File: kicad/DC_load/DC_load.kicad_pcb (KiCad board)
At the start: 2 copper layers, 110 x 145 mm, 217 parts, among them J1 BNC, J10 DC fan connector, J2 red_terminal, J3 red terminal, J4 black terminal, J5 black terminal, J6 USB_B, J8 FT232 programming port, J9 Conn_01x04_Socket, Q1 MMBT5401, Q10 MMBT5401, Q11 MMBT5551L, Q12 MMBT5401, Q13 AO3400A, Q14 MMBT5551L, Q2 MMBT5401, Q3 FQP19N20C, Q4 FQP19N20C, Q5 FQP19N20C, Q6 FQP19N20C, Q7 MMBT5551L, Q8 MMBT5401, Q9 MMBT5551L, SW1 RotaryEncoder_Switch, SW2 RotaryEncoder_Switch, SW3 SW_Push, SW8 SW_Push, U1 FSA3157P6X, U10 FSA3157P6X, U11 FSA3157P6X, U12 FSA3157P6X, U13 TLV9062, U14 AMS1117-3.3, U15 74HC14D653, U16 93LCxxB, U17 CH340C, U18 TL431DBZ, U19 INA181, U2 Screen, U20 INA181, U21 INA181, U22 INA181, U5 TLV9062, U6 TLV9062, U7 LMT84LPM, U8 STM32F103C8Tx, U9 Front plate

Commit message: Još gate driver layout.
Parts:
- removed TP10: TestPoint, TestPoint:TestPoint_Pad_D2.0mm
- moved JP3 6.55 mm to (95.1, 117.4), turned to 180 degrees
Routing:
- net /Microcontroller/BNC_CONTROL: track 120.8 -> 45.8 mm
- net CTRL_SEL: track 186.1 -> 117.3 mm
- net FAN_PWM: track 0.00 -> 61.4 mm, vias 0 -> 3
- net 3V3: track 113.0 -> 104.5 mm
- net /Microcontroller/CH3_MEAS: track 138.2 -> 130.0 mm
- net CH1_CONTROL: track 6.50 -> 0.00 mm
- net Net-(C26-Pad2): track 103.6 -> 97.4 mm
- net 5V: track 102.7 -> 96.6 mm
- net CH2_CONTROL: track 4.52 -> 0.00 mm
- net Net-(Q3-S): track 6.17 -> 3.48 mm
- net Net-(Q6-S): track 6.24 -> 4.31 mm
- net GND: track 120.3 -> 119.2 mm
- net Net-(R22-Pad2): track 29.8 -> 28.8 mm
- net Net-(R23-Pad2): track 30.6 -> 29.7 mm
- net Net-(Q5-S): track 3.65 -> 2.93 mm
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
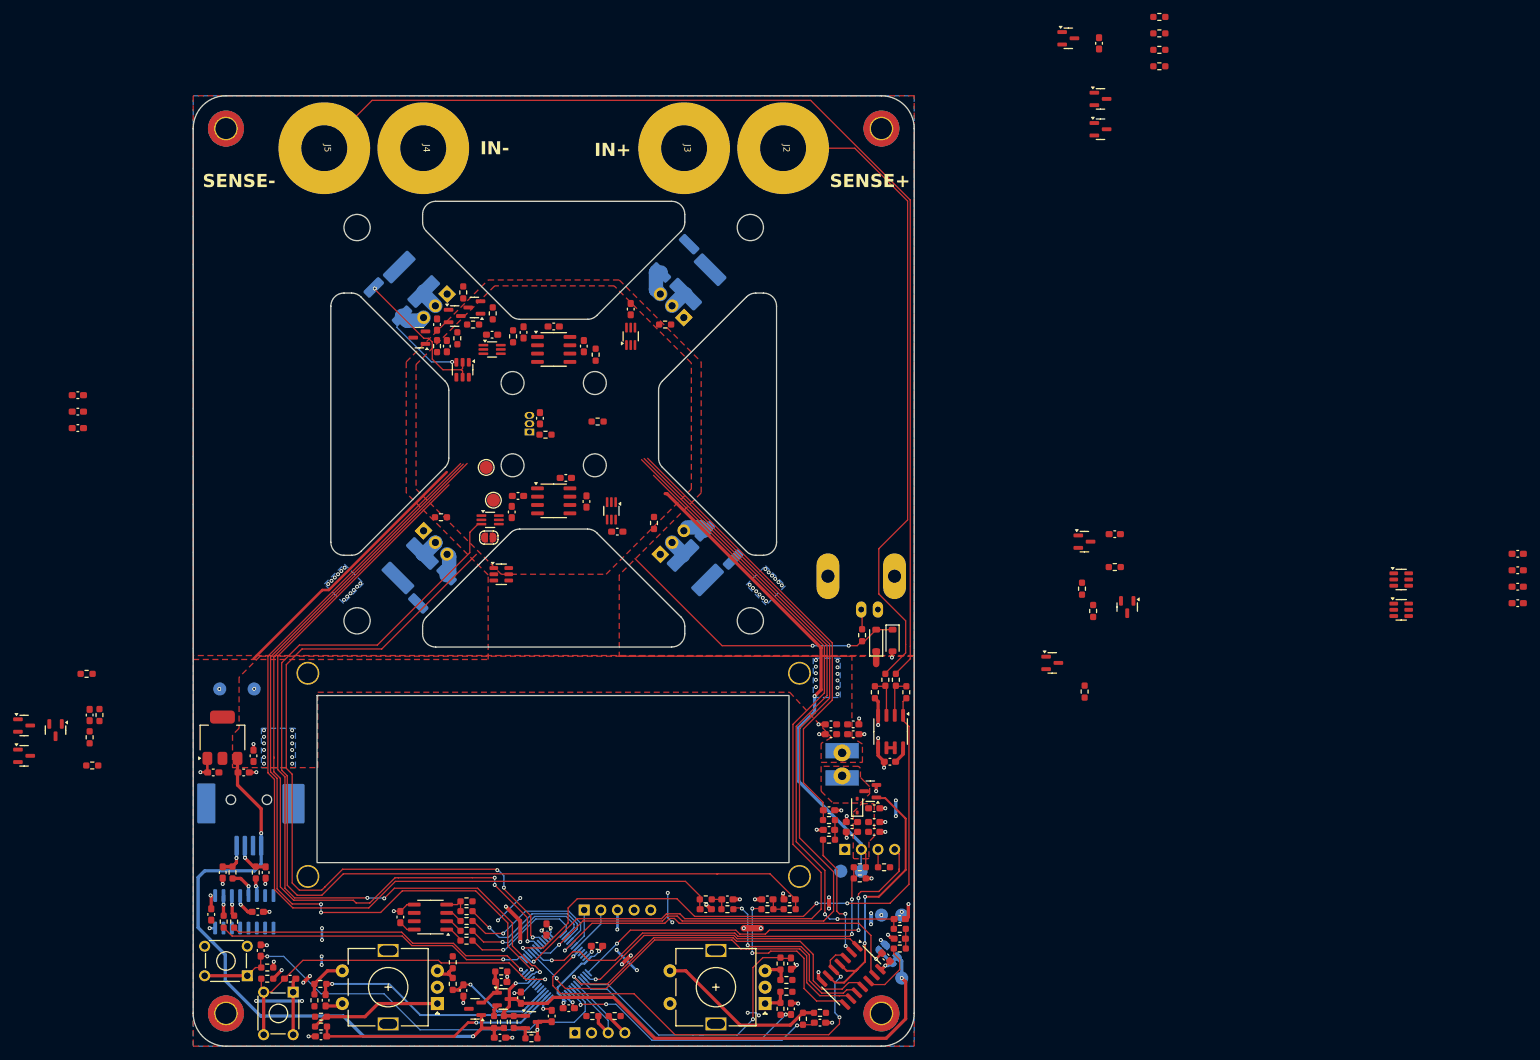
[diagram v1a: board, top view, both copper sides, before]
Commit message: RC filter na ADC linijama Placement update.
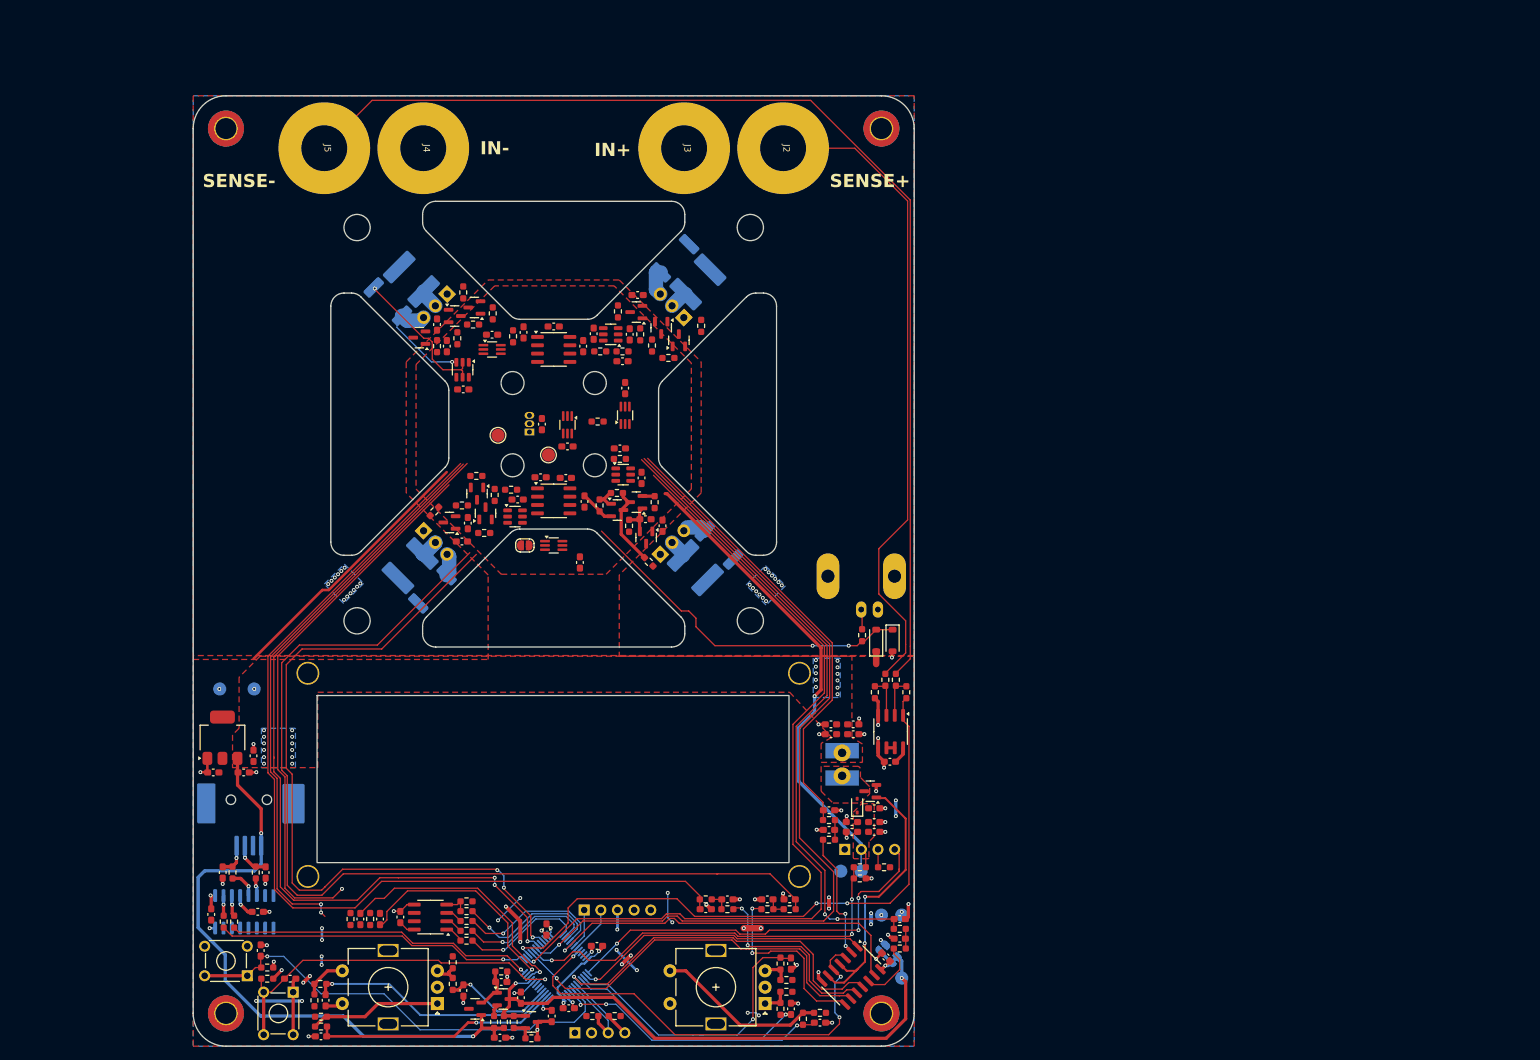
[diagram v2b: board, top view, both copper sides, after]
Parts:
- added C70: 1n, Capacitor_SMD:C_0603_1608Metric_Pad1.08x0.95mm_HandSolder, F.Cu at (115.5, 90.5)
- added C71: 1n, Capacitor_SMD:C_0603_1608Metric_Pad1.08x0.95mm_HandSolder, F.Cu at (115.1, 103.8)
- added C72: 1n, Capacitor_SMD:C_0603_1608Metric_Pad1.08x0.95mm_HandSolder, F.Cu at (78.5, 175.6)
- added C73: 1n, Capacitor_SMD:C_0603_1608Metric_Pad1.08x0.95mm_HandSolder, F.Cu at (75.5, 175.6)
- added R75: 10k, Resistor_SMD:R_0603_1608Metric_Pad0.98x0.95mm_HandSolder, F.Cu at (74.0, 175.6)
- added R76: 10k, Resistor_SMD:R_0603_1608Metric_Pad0.98x0.95mm_HandSolder, F.Cu at (77.0, 175.6)
- added R77: 10k, Resistor_SMD:R_0603_1608Metric_Pad0.98x0.95mm_HandSolder, F.Cu at (115.1, 105.4)
- added R78: 10k, Resistor_SMD:R_0603_1608Metric_Pad0.98x0.95mm_HandSolder, F.Cu at (115.5, 89.0)
- moved C9 162.8 mm to (91.2, 94.8)
- moved C65 153.4 mm to (99.5, 111.6)
- moved C46 145.5 mm to (111.1, 86.3), turned to -90 degrees
- moved C64 134.7 mm to (118.4, 108.3), turned to 90 degrees
- moved U22 127.7 mm to (113.7, 86.4), turned to 180 degrees
- moved U21 119.8 mm to (115.6, 107.8)
- moved R71 92.8 mm to (118.2, 86.4), turned to -90 degrees
- moved C68 90.9 mm to (121.6, 115.6), turned to -90 degrees
- moved R72 90.9 mm to (120.0, 88.1), turned to -90 degrees
- moved R74 90.7 mm to (114.8, 82.9), turned to -90 degrees
- moved R73 88.4 mm to (122.5, 90.0)
- moved C67 84.7 mm to (116.6, 86.4), turned to -90 degrees
- moved C7 80.2 mm to (117.8, 80.4), turned to 0 degrees
- moved Q7 79.8 mm to (93.3, 110.7), turned to -90 degrees
- moved D8 78.0 mm to (117.6, 83.0), turned to 180 degrees
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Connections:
- net /Microcontroller/PROG_RX renamed PROG_RX
- net /Microcontroller/PROG_TX renamed PROG_TX
- C16 pad 2: 5V -> 3V3
- C17 pad 2: 5V -> 3V3
- C18 pad 2: 5V -> 3V3
- C19 pad 2: 5V -> 3V3
- U1 pad 5: 5V -> 3V3
- U10 pad 5: 5V -> 3V3
- U11 pad 5: 5V -> 3V3
- U12 pad 5: 5V -> 3V3
- U8 pad 10: /Microcontroller/CH1_MEAS -> Net-(U8-PA0)
- U8 pad 11: /Microcontroller/CH2_MEAS -> Net-(U8-PA1)
- U8 pad 14: /Microcontroller/CH3_MEAS -> Net-(U8-PA4)
- U8 pad 18: /Microcontroller/CH4_MEAS -> Net-(U8-PB0)
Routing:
- net Net-(U8-PB0): track 0.00 -> 133.8 mm
- net /Microcontroller/CH4_MEAS: track 133.8 -> 0.00 mm
- net Net-(U8-PA4): track 0.00 -> 130.0 mm
- net /Microcontroller/CH3_MEAS: track 130.0 -> 0.00 mm
- net /Microcontroller/CH2_MEAS: track 128.1 -> 0.00 mm, vias 3 -> 1
- net Net-(U8-PA1): track 0.00 -> 121.2 mm, vias 0 -> 2
- net /Microcontroller/CH1_MEAS: track 122.5 -> 82.7 mm, vias 3 -> 2
- net Net-(U8-PA0): track 0.00 -> 38.5 mm
- net Net-(Q8-C): track 0.00 -> 12.0 mm
- net /Microcontroller/BNC_CONTROL: track 45.8 -> 53.4 mm
- net Net-(D4-A): track 0.00 -> 5.77 mm
- net Net-(C22-Pad2): track 157.7 -> 152.9 mm
- net Net-(Q9-E): track 0.00 -> 4.73 mm
- net Net-(Q9-B): track 0.00 -> 3.56 mm
- net Net-(Q8-E): track 0.00 -> 1.81 mm

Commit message: Done???.
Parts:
- added C74: 1n, Capacitor_SMD:C_0603_1608Metric_Pad1.08x0.95mm_HandSolder, F.Cu at (151.1, 141.0)
- added C75: 1n, Capacitor_SMD:C_0603_1608Metric_Pad1.08x0.95mm_HandSolder, F.Cu at (159.0, 141.0)
- moved C17 28.2 mm to (95.3, 96.5), turned to 0 degrees
- moved U1 22.1 mm to (95.4, 98.7)
- moved JP3 21.8 mm to (91.7, 98.7), turned to -90 degrees
- moved C18 12.4 mm to (103.8, 95.8), turned to 180 degrees
- moved U10 9.50 mm to (103.8, 93.5), turned to 180 degrees
- moved TP8 9.42 mm to (95.3, 101.7)
- moved C19 5.28 mm to (114.2, 99.6), turned to 0 degrees
- moved TP9 4.11 mm to (95.2, 105.7)
- moved R74 3.97 mm to (117.8, 80.3), turned to 180 degrees
- moved C7 3.75 mm to (115.1, 83.0), turned to 90 degrees
- moved C64 3.68 mm to (115.9, 105.6), turned to 0 degrees
- moved R10 3.40 mm to (111.6, 103.1), turned to 180 degrees
- moved R5 3.02 mm to (100.2, 89.4)
- moved U12 2.48 mm to (115.1, 96.4), turned to -90 degrees
- moved R77 2.31 mm to (114.9, 103.1)
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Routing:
- net /Microcontroller/CH2_MEAS: track 0.00 -> 121.0 mm, vias 1 -> 4
- net 12V: track 76.0 -> 190.2 mm, vias 1 -> 9
- net GND: track 119.2 -> 222.7 mm, vias 60 -> 98
- net Net-(U8-PA1): track 121.2 -> 35.6 mm, vias 2 -> 1
- net CTRL_SEL: track 117.3 -> 172.2 mm, vias 3 -> 7
- net /Microcontroller/BNC_CONTROL: track 53.4 -> 103.4 mm, vias 2 -> 11
- net 3V3: track 104.5 -> 150.3 mm, vias 27 -> 39
- net Net-(Q14-E): track 0.00 -> 22.3 mm, vias 0 -> 2
- net CH1_CONTROL: track 0.00 -> 21.7 mm, vias 0 -> 4
- net Net-(C22-Pad2): track 152.9 -> 173.8 mm, vias 0 -> 2
- net Net-(C24-Pad2): track 147.9 -> 168.4 mm, vias 0 -> 2
- net Net-(C26-Pad2): track 97.4 -> 116.6 mm, vias 2 -> 4
- net Net-(U8-PB0): track 133.8 -> 151.3 mm, vias 0 -> 1
- net Net-(C28-Pad2): track 70.2 -> 87.6 mm, vias 0 -> 2
- net /Microcontroller/CH1_MEAS: track 82.7 -> 99.9 mm
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
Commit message: Ready for production.
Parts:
- removed U9: Front plate, DC_load:front_plate
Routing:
- net /Microcontroller/BNC_CONTROL: track 103.4 -> 102.5 mm

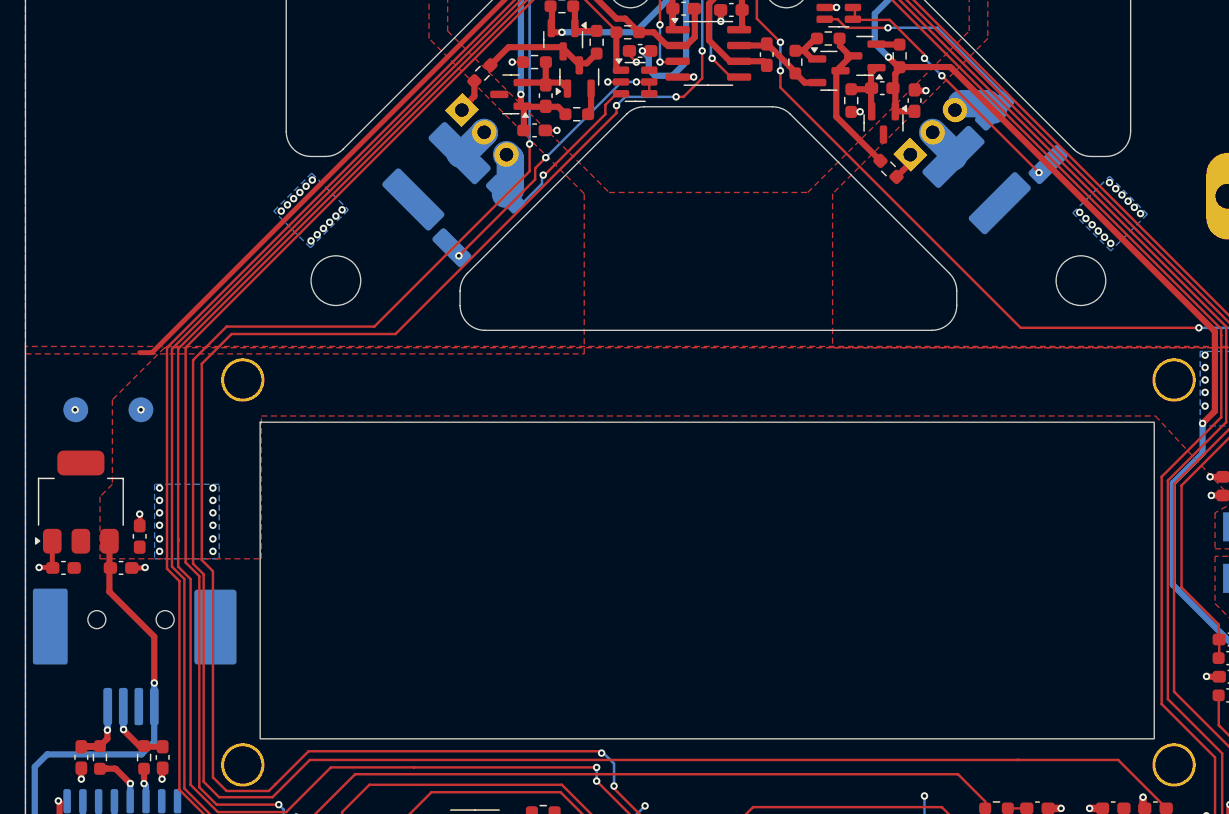
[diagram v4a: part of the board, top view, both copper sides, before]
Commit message: Galvanic isolation for the UART.
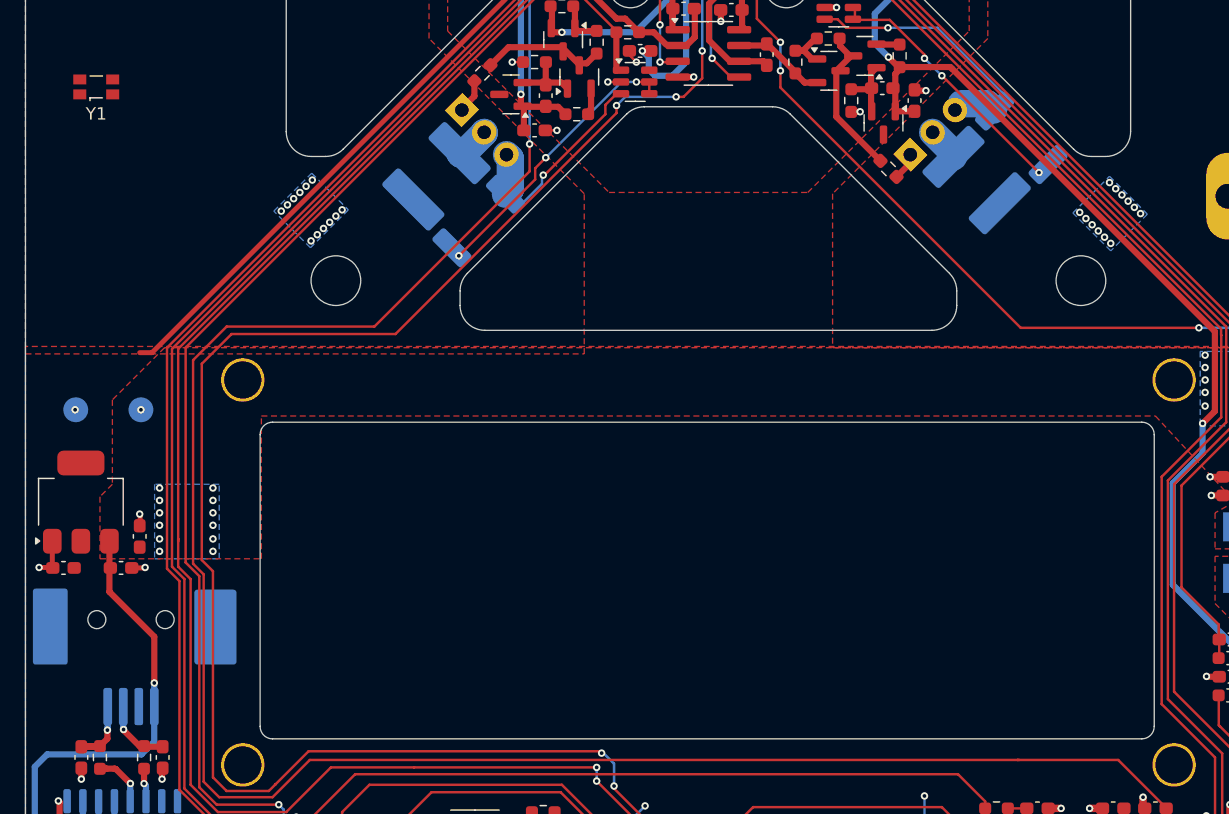
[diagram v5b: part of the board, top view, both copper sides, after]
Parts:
- added Y1: SG-3030CM, Oscillator:Oscillator_SMD_SeikoEpson_SG3030CM, F.Cu at (55.7, 114.5)

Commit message: Sim, comp, power.
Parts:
- removed C54, C56, C58, C59, C60, C61, C62, C63: 10u, Capacitor_SMD:C_0603_1608Metric_Pad1.08x0.95mm_HandSolder
- removed C55: 100n, Capacitor_SMD:C_0603_1608Metric_Pad1.08x0.95mm_HandSolder
- removed D5: 1N5819WS, Diode_SMD:D_SOD-323
- removed L4: 4.7u, DC_load:L_Bourns_SRN6045TA
- removed Q13: AO3400A, Package_TO_SOT_SMD:SOT-23
- removed R65: 10k, Resistor_SMD:R_0603_1608Metric_Pad0.98x0.95mm_HandSolder
- removed R66: 49.9k, Resistor_SMD:R_0603_1608Metric_Pad0.98x0.95mm_HandSolder
- removed Y1: SG-3030CM, Oscillator:Oscillator_SMD_SeikoEpson_SG3030CM
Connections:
- U15 pad 3: FAN_BOOST -> (no net)
- U15 pad 4: Net-(Q13-G) -> (no net)
- U15 pad 5: FAN_BOOST -> (no net)
- U15 pad 6: Net-(Q13-G) -> (no net)
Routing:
- net Net-(Q13-G): track 41.5 -> 0.00 mm, vias 2 -> 0
- net (no net): track 0.00 -> 41.5 mm, vias 0 -> 2
- added copper zone on F.Cu, net (none)
- removed copper zone on F.Cu, net /Microcontroller/FAN_DRAIN
